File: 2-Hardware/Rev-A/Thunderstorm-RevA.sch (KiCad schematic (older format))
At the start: 21 parts, among them SW1 SWITCH_SPDT, U1 M10382, U2 LM358

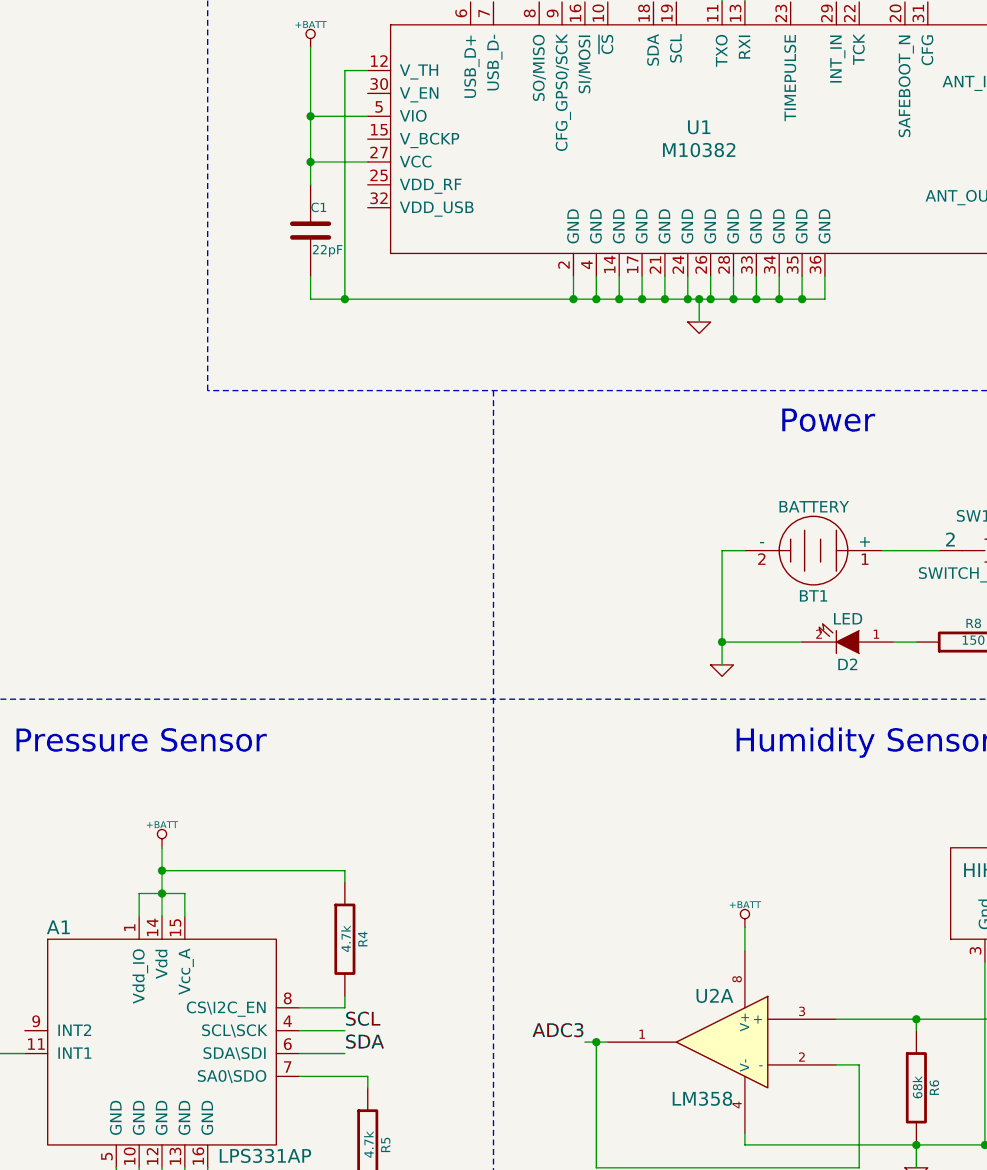
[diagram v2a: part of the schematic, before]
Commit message: Added decoupling capacitors.
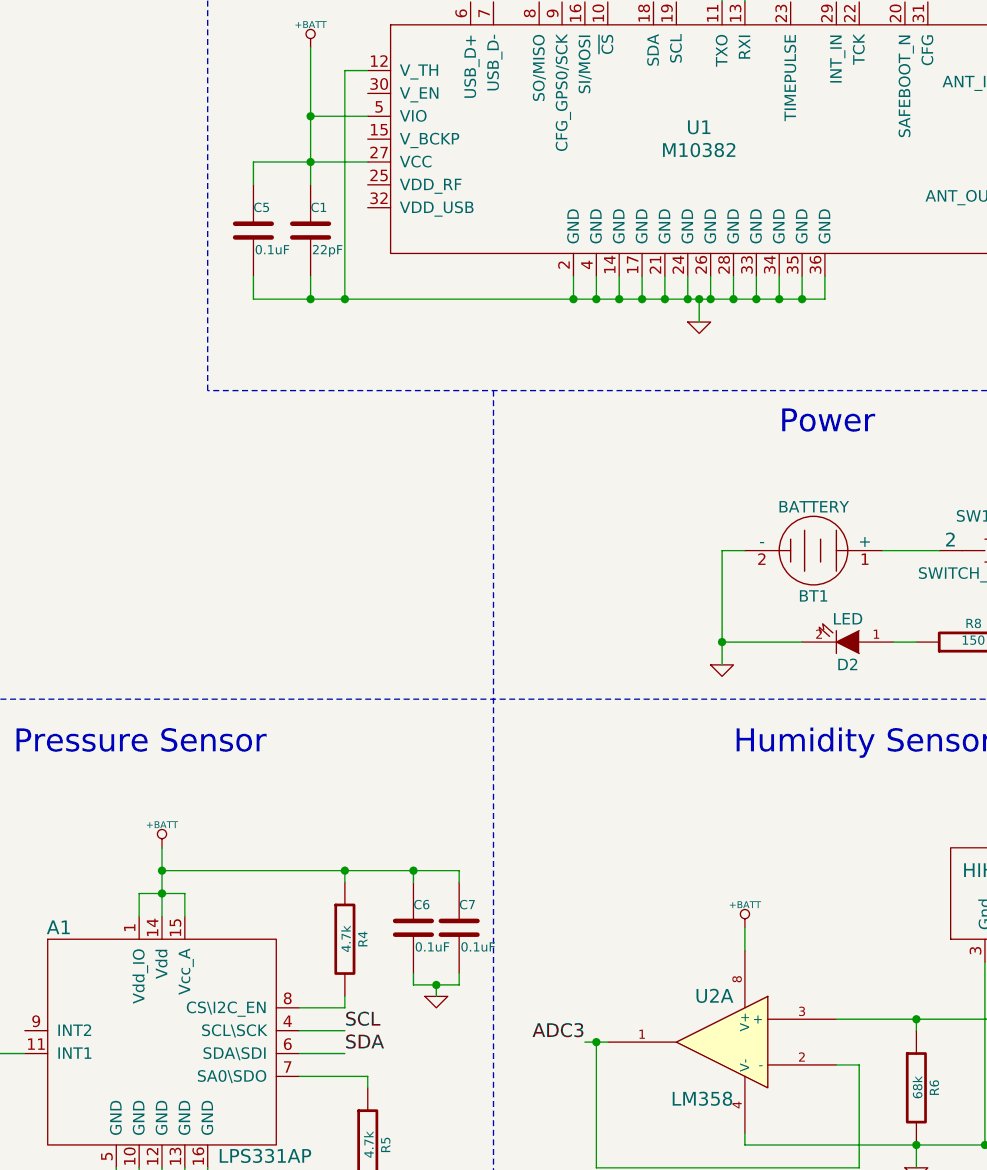
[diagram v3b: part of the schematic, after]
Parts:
- added C5, C6, C7: 0.1uF, ~, symbol C
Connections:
- net +BATT: now also C5.1, C6.1, C7.1
- net GND: now also C5.2, C6.2, C7.2
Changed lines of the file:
@@
 Sheet 1 1
 Title ""
-Date "28 may 2014"
+Date "30 may 2014"
 Rev ""
 Comp ""
@@
 $EndComp
 $Comp
-L GND #PWR12
+L GND #PWR01
 U 1 1 537AB6FC
 P 9200 4550
-F 0 "#PWR12" H 9200 4550 30  0001 C CNN
+F 0 "#PWR01" H 9200 4550 30  0001 C CNN
 F 1 "GND" H 9200 4480 30  0001 C CNN
 F 2 "" H 9200 4550 60  0000 C CNN
@@
 	10600 3950 10600 4450
 $Comp
-L +BATT #PWR15
+L +BATT #PWR02
 U 1 1 537AB71B
 P 10600 3950
-F 0 "#PWR15" H 10600 3900 20  0001 C CNN
+F 0 "#PWR02" H 10600 3900 20  0001 C CNN
 F 1 "+BATT" H 10600 4050 30  0000 C CNN
 F 2 "" H 10600 3950 60  0000 C CNN
@@
 $EndComp
 $Comp
-L +BATT #PWR6
+L +BATT #PWR03
 U 1 1 537AB72A
 P 4050 6000
-F 0 "#PWR6" H 4050 5950 20  0001 C CNN
+F 0 "#PWR03" H 4050 5950 20  0001 C CNN
 F 1 "+BATT" H 4050 6100 30  0000 C CNN
 F 2 "" H 4050 6000 60  0000 C CNN
@@
 	4050 6300 3400 6300
 $Comp
-L GND #PWR5
+L GND #PWR04
 U 1 1 537AB73F
 P 3600 5900
-F 0 "#PWR5" H 3600 5900 30  0001 C CNN
+F 0 "#PWR04" H 3600 5900 30  0001 C CNN
 F 1 "GND" H 3600 5830 30  0001 C CNN
 F 2 "" H 3600 5900 60  0000 C CNN
@@
 $EndComp
 $Comp
-L GND #PWR4
+L GND #PWR05
 U 1 1 537AB74E
 P 2050 5950
-F 0 "#PWR4" H 2050 5950 30  0001 C CNN
+F 0 "#PWR05" H 2050 5950 30  0001 C CNN
 F 1 "GND" H 2050 5880 30  0001 C CNN
 F 2 "" H 2050 5950 60  0000 C CNN
@@
 $EndComp
 $Comp
-L +BATT #PWR2
+L +BATT #PWR06
 U 1 1 537AB819
 P 1600 5400
-F 0 "#PWR2" H 1600 5350 20  0001 C CNN
+F 0 "#PWR06" H 1600 5350 20  0001 C CNN
 F 1 "+BATT" H 1600 5500 30  0000 C CNN
 F 2 "" H 1600 5400 60  0000 C CNN
@@
 $EndComp
 $Comp
-L GND #PWR11
+L GND #PWR07
 U 1 1 537AB9B0
 P 9100 3050
-F 0 "#PWR11" H 9100 3050 30  0001 C CNN
+F 0 "#PWR07" H 9100 3050 30  0001 C CNN
 F 1 "GND" H 9100 2980 30  0001 C CNN
 F 2 "" H 9100 3050 60  0000 C CNN
@@
 	8550 2950 8550 2850
 Wire Wire Line
-	7400 2950 9650 2950
+	7150 2950 9650 2950
 Wire Wire Line
 	9650 2950 9650 2850
@@
 Connection ~ 9550 2950
 $Comp
-L +BATT #PWR10
+L +BATT #PWR08
 U 1 1 537ABBDB
 P 7400 1850
-F 0 "#PWR10" H 7400 1800 20  0001 C CNN
+F 0 "#PWR08" H 7400 1800 20  0001 C CNN
 F 1 "+BATT" H 7400 1950 30  0000 C CNN
 F 2 "" H 7400 1850 60  0000 C CNN
@@
 $EndComp
 Wire Wire Line
-	7400 2350 7650 2350
+	7150 2350 7650 2350
 Wire Wire Line
 	7400 1850 7400 2450
@@
 Connection ~ 10050 6650
 $Comp
-L GND #PWR14
+L GND #PWR09
 U 1 1 537AC1B6
 P 10050 6750
-F 0 "#PWR14" H 10050 6750 30  0001 C CNN
+F 0 "#PWR09" H 10050 6750 30  0001 C CNN
 F 1 "GND" H 10050 6680 30  0001 C CNN
 F 2 "" H 10050 6750 60  0000 C CNN
@@
 	10050 6650 10050 6750
 $Comp
-L +BATT #PWR16
+L +BATT #PWR010
 U 1 1 537AC216
 P 10850 5800
-F 0 "#PWR16" H 10850 5750 20  0001 C CNN
+F 0 "#PWR010" H 10850 5750 20  0001 C CNN
 F 1 "+BATT" H 10850 5900 30  0000 C CNN
 F 2 "" H 10850 5800 60  0000 C CNN
@@
 $EndComp
 $Comp
-L +BATT #PWR13
+L +BATT #PWR011
 U 1 1 537AC225
 P 9300 5700
-F 0 "#PWR13" H 9300 5650 20  0001 C CNN
+F 0 "#PWR011" H 9300 5650 20  0001 C CNN
 F 1 "+BATT" H 9300 5800 30  0000 C CNN
 F 2 "" H 9300 5700 60  0000 C CNN
@@
 $EndComp
 $Comp
-L GND #PWR9
+L GND #PWR012
 U 1 1 537ACB4C
 P 6750 7050
-F 0 "#PWR9" H 6750 7050 30  0001 C CNN
+F 0 "#PWR012" H 6750 7050 30  0001 C CNN
 F 1 "GND" H 6750 6980 30  0001 C CNN
 F 2 "" H 6750 7050 60  0000 C CNN
@@
 	7550 5500 7550 5450
 Wire Wire Line
-	7550 5450 6750 5450
+	6750 5450 8050 5450
 Wire Wire Line
 	6750 5350 6750 5650
 $Comp
-L +BATT #PWR8
+L +BATT #PWR013
 U 1 1 537ACEB8
 P 6750 5350
-F 0 "#PWR8" H 6750 5300 20  0001 C CNN
+F 0 "#PWR013" H 6750 5300 20  0001 C CNN
 F 1 "+BATT" H 6750 5450 30  0000 C CNN
 F 2 "" H 6750 5350 60  0000 C CNN
@@
 Connection ~ 8650 6200
 $Comp
-L +BATT #PWR3
+L +BATT #PWR014
 U 1 1 53851E13
 P 1800 6650
-F 0 "#PWR3" H 1800 6600 20  0001 C CNN
+F 0 "#PWR014" H 1800 6600 20  0001 C CNN
 F 1 "+BATT" H 1800 6750 30  0000 C CNN
 F 2 "" H 1800 6650 60  0000 C CNN
@@
 $EndComp
 $Comp
-L GND #PWR7
+L GND #PWR015
 U 1 1 5385237F
 P 4050 6800
-F 0 "#PWR7" H 4050 6800 30  0001 C CNN
+F 0 "#PWR015" H 4050 6800 30  0001 C CNN
 F 1 "GND" H 4050 6730 30  0001 C CNN
 F 2 "" H 4050 6800 60  0000 C CNN
@@
 $EndComp
 $Comp
-L GND #PWR1
+L GND #PWR016
 U 1 1 538677C7
 P 1000 7450
-F 0 "#PWR1" H 1000 7450 30  0001 C CNN
+F 0 "#PWR016" H 1000 7450 30  0001 C CNN
 F 1 "GND" H 1000 7380 30  0001 C CNN
 F 2 "" H 1000 7450 60  0000 C CNN
@@
 Wire Wire Line
 	1000 6300 1000 6350
+$Comp
+L C C5
+U 1 1 5387DC6E
+P 7150 2650
+F 0 "C5" H 7150 2750 40  0000 L CNN
+F 1 "0.1uF" H 7156 2565 40  0000 L CNN
+F 2 "~" H 7188 2500 30  0000 C CNN
+F 3 "~" H 7150 2650 60  0000 C CNN
+	1    7150 2650
+	1    0    0    -1
+$EndComp
+Wire Wire Line
+	7150 2450 7150 2350
+Wire Wire Line
+	7150 2850 7150 2950
+Connection ~ 7400 2950
+$Comp
+L C C6
+U 1 1 5387E08C
+P 7850 5700
+F 0 "C6" H 7850 5800 40  0000 L CNN
+F 1 "0.1uF" H 7856 5615 40  0000 L CNN
+F 2 "~" H 7888 5550 30  0000 C CNN
+F 3 "~" H 7850 5700 60  0000 C CNN
+	1    7850 5700
+	1    0    0    -1
+$EndComp
+$Comp
+L C C7
+U 1 1 5387E09B
+P 8050 5700
+F 0 "C7" H 8050 5800 40  0000 L CNN
+F 1 "0.1uF" H 8056 5615 40  0000 L CNN
+F 2 "~" H 8088 5550 30  0000 C CNN
+F 3 "~" H 8050 5700 60  0000 C CNN
+	1    8050 5700
+	1    0    0    -1
+$EndComp
+$Comp
+L GND #PWR017
+U 1 1 5387E0AA
+P 7950 6000
+F 0 "#PWR017" H 7950 6000 30  0001 C CNN
+F 1 "GND" H 7950 5930 30  0001 C CNN
+F 2 "" H 7950 6000 60  0000 C CNN
+F 3 "" H 7950 6000 60  0000 C CNN
+	1    7950 6000
+	1    0    0    -1
+$EndComp
+Wire Wire Line
+	7850 5900 7850 5950
+Wire Wire Line
+	7850 5950 8050 5950
+Wire Wire Line
+	8050 5950 8050 5900
+Wire Wire Line
+	7950 5950 7950 6000
+Connection ~ 7950 5950
+Wire Wire Line
+	8050 5450 8050 5500
+Connection ~ 7550 5450
+Wire Wire Line
+	7850 5500 7850 5450
+Connection ~ 7850 5450
 $EndSCHEMATC

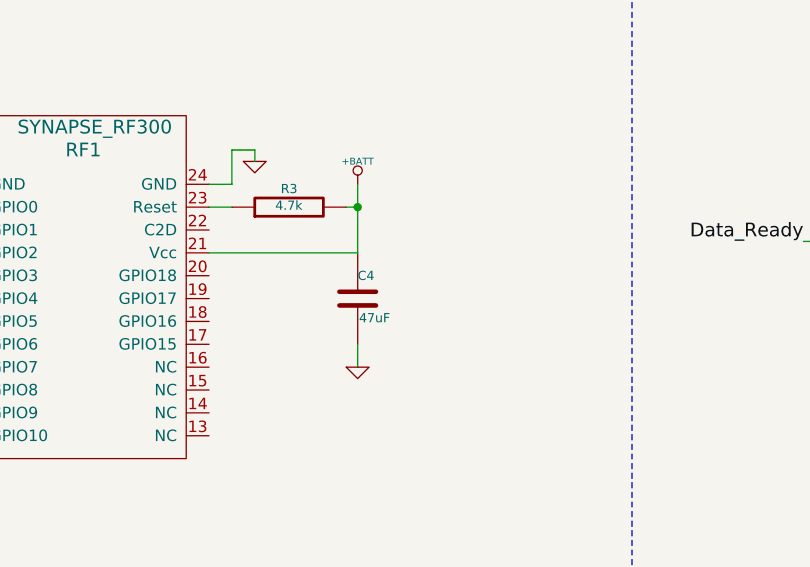
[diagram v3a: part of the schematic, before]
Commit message: Added decoupling capacitor.
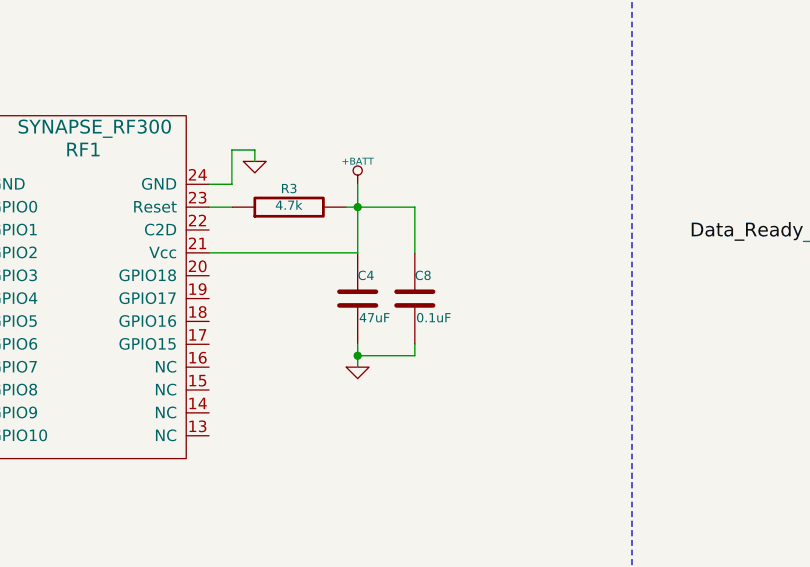
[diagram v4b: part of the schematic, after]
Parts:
- added C8: 0.1uF, ~, symbol C
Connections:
- net +BATT: now also C8.1
- net GND: now also C8.2
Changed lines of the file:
@@
 Sheet 1 1
 Title ""
-Date "30 may 2014"
+Date "1 jun 2014"
 Rev ""
 Comp ""
@@
 	4050 6000 4050 6300
 Wire Wire Line
-	4050 6100 4000 6100
+	4000 6100 4300 6100
 Connection ~ 4050 6100
 Wire Wire Line
@@
 	7850 5500 7850 5450
 Connection ~ 7850 5450
+$Comp
+L C C8
+U 1 1 538B9DCE
+P 4300 6500
+F 0 "C8" H 4300 6600 40  0000 L CNN
+F 1 "0.1uF" H 4306 6415 40  0000 L CNN
+F 2 "~" H 4338 6350 30  0000 C CNN
+F 3 "~" H 4300 6500 60  0000 C CNN
+	1    4300 6500
+	1    0    0    -1
+$EndComp
+Wire Wire Line
+	4300 6100 4300 6300
+Wire Wire Line
+	4300 6700 4300 6750
+Wire Wire Line
+	4300 6750 4050 6750
+Connection ~ 4050 6750
 $EndSCHEMATC
